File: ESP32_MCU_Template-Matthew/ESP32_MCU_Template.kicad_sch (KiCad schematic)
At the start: 43 parts, among them IC1 ESP32-S3-WROOM-1-N8R8, IC2 CP2102N-A02-GQFN28, IC3 TLP175A_TPL,E, IC4 TPS2116DRLR, IC5 MIC37100-3.3WS, J1 ESP_USB, Q1 MMBT2222LT1G, Q2 MMBT2222LT1G, U1 USBLC6-2SC6, U2 SN65HVD230

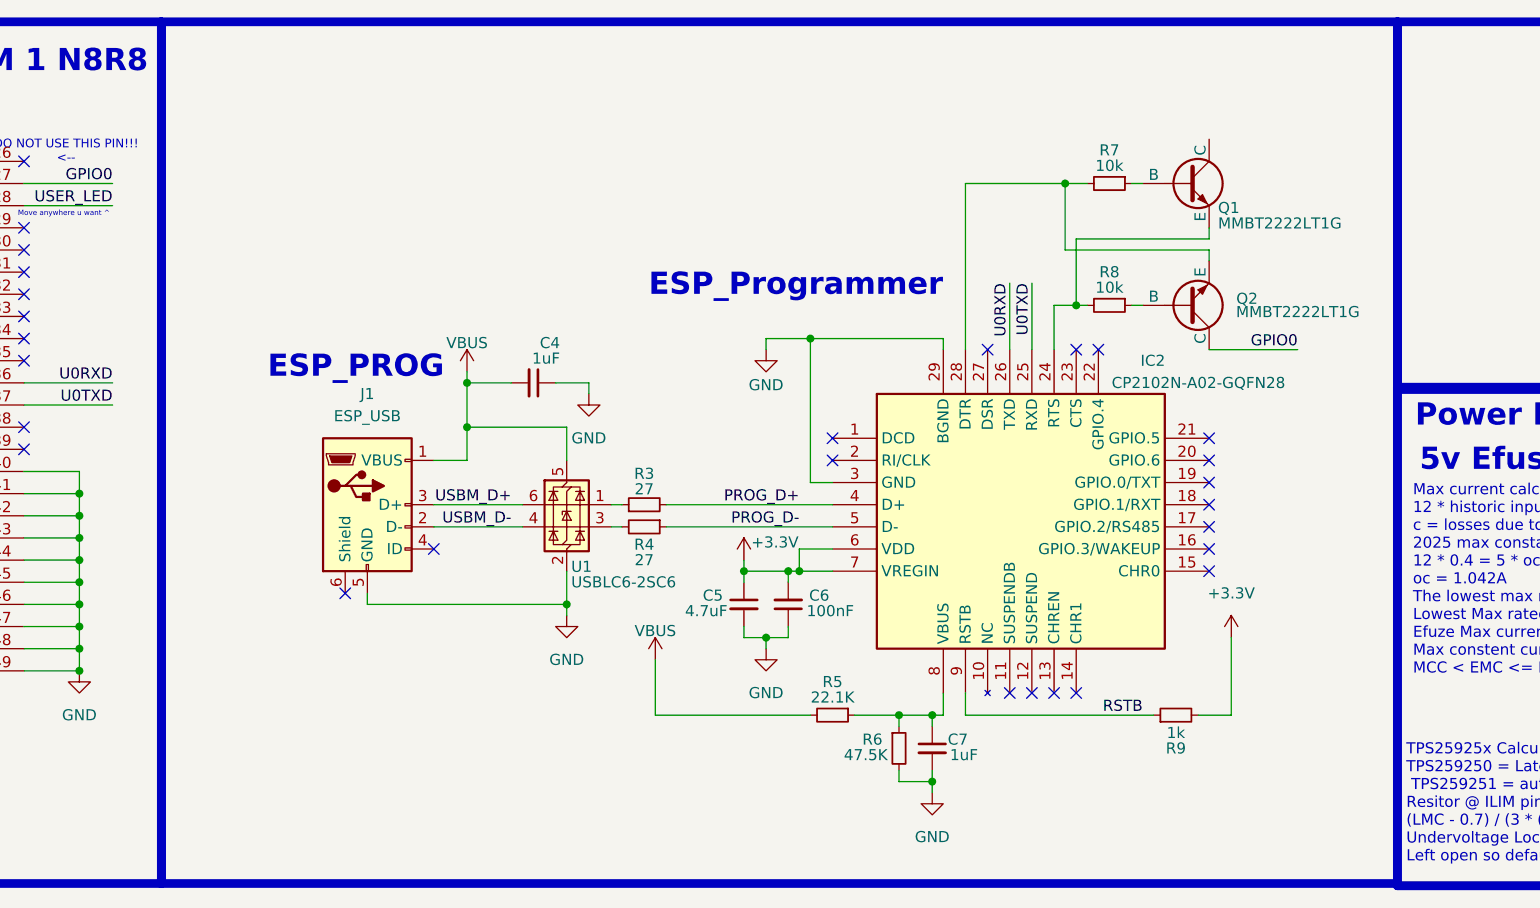
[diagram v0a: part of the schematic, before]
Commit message: ESP32 MCU update
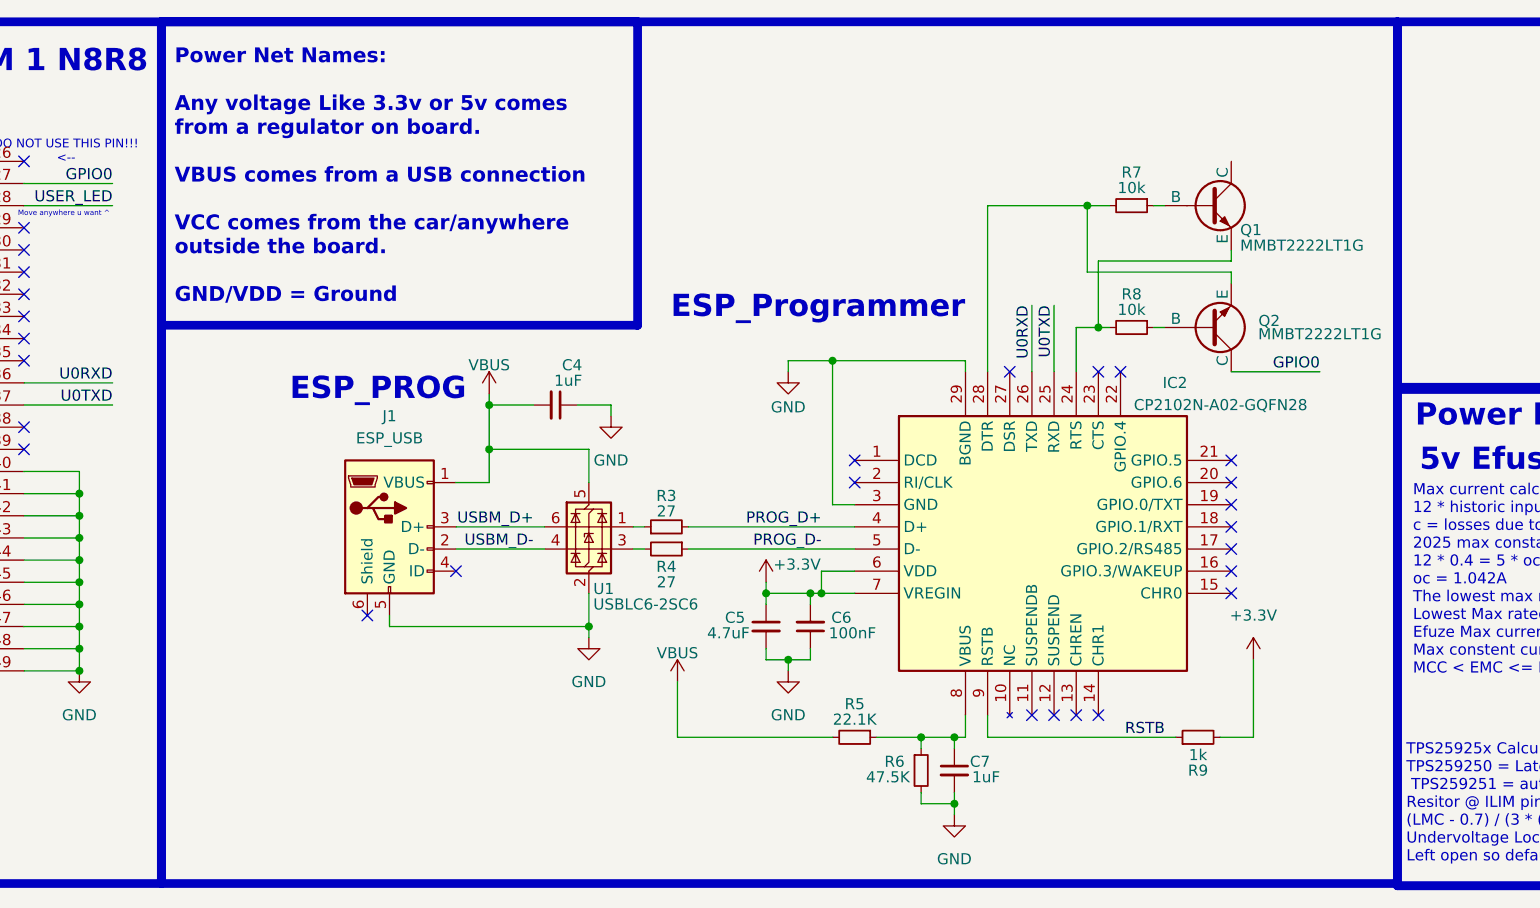
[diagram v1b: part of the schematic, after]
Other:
- note added: "Power Net Names: Any voltage Like 3.3v or 5v comes from a regulator on board. VBUS comes from a USB connection VCC comes from the car/anywhere outside the board. GND/VDD = Ground"
- moved on the sheet: C4, C5, C6, C7, IC2, J1, Q1, Q2, R3, R4, R5, R6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
